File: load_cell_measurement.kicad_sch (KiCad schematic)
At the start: 15 parts, among them IC1 MCP3561R-E_ST, J8 Conn_01x04_Pin

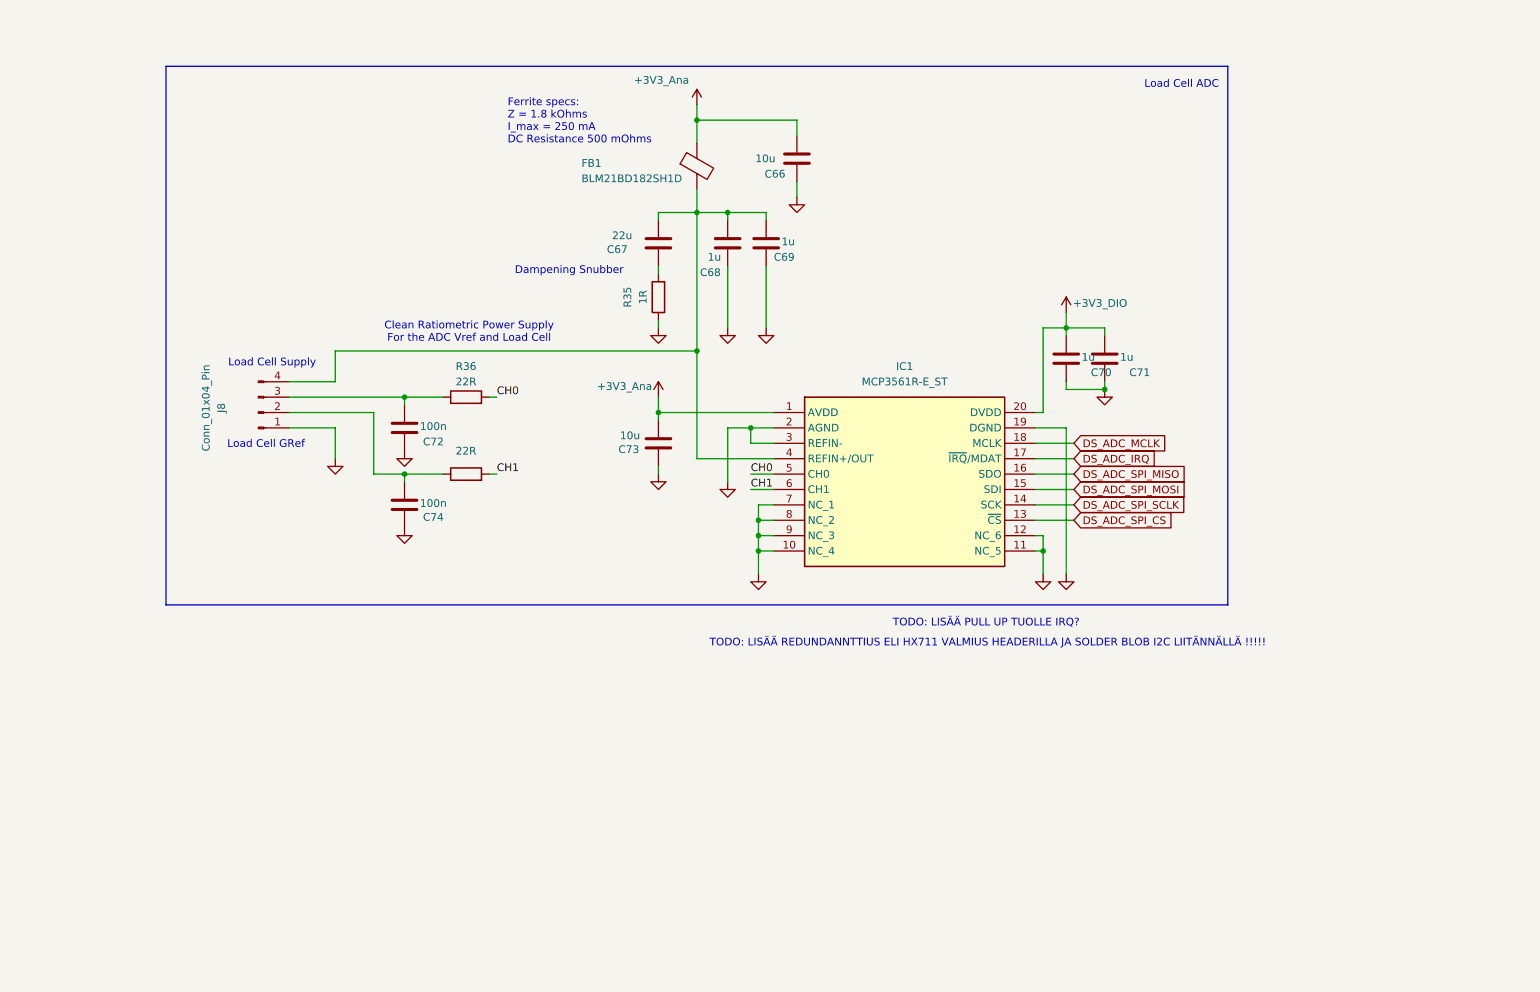
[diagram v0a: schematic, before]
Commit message: Switched isolating opamp. Switched Isolating DCDC converter. Minor layout improvements. Added load cell ADC.
[KiCad Version: 10.0.4]
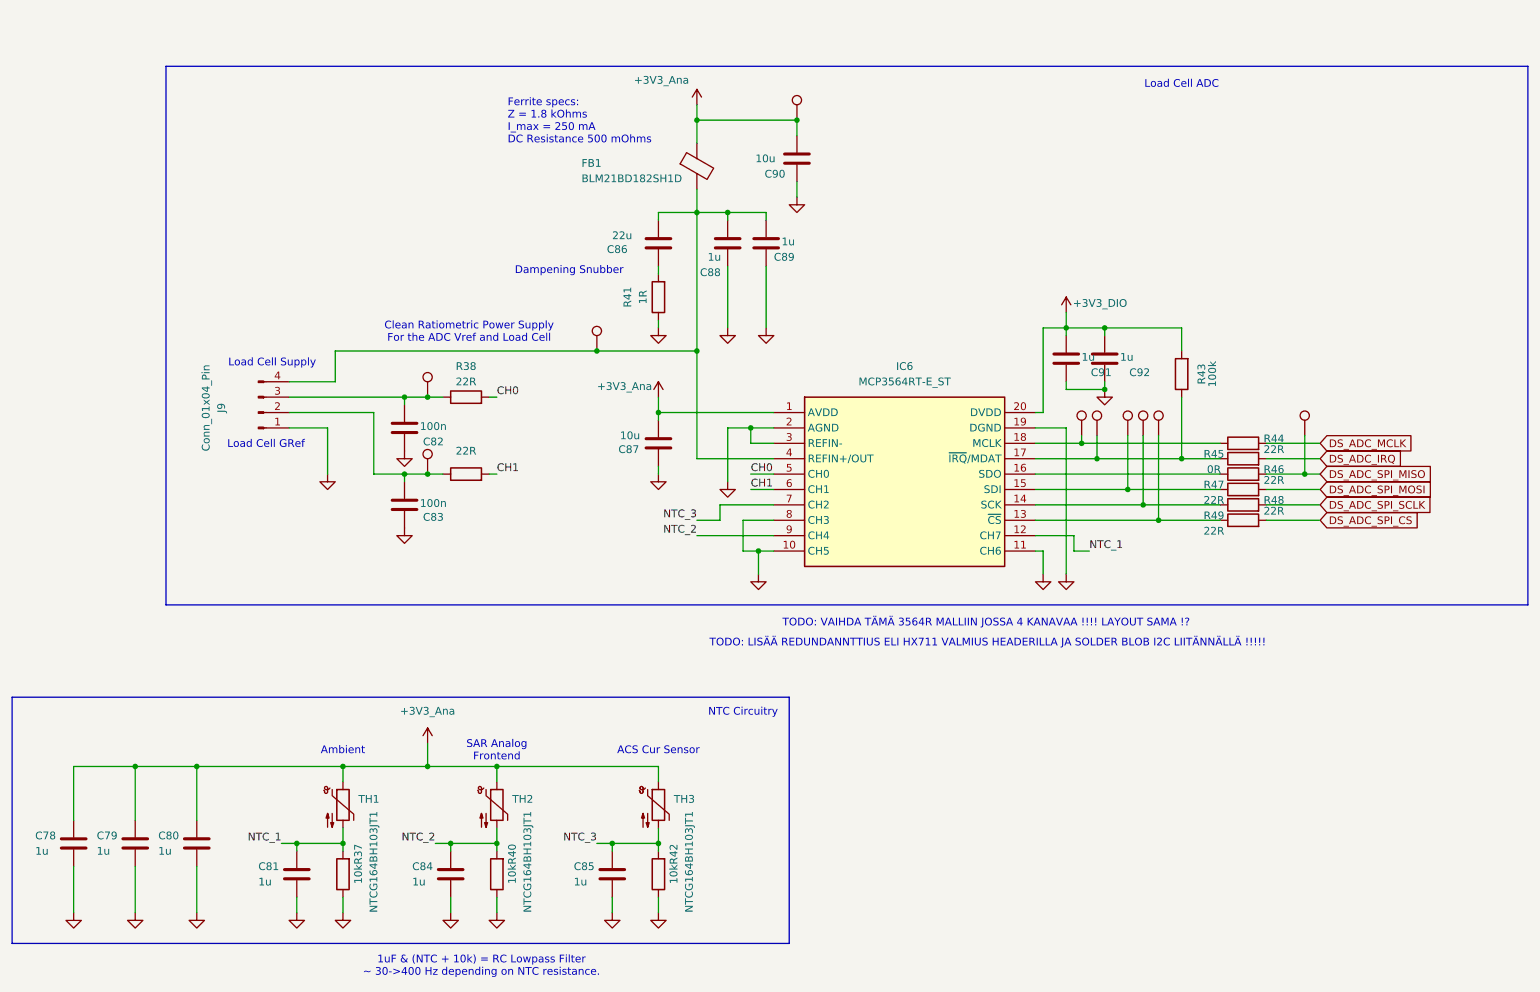
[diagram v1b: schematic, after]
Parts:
- removed IC1: MCP3561R-E_ST, SamacSys_Parts:SOP65P640X120-20N, symbol SamacSys_Parts:MCP3561R-E_ST
- added C78, C79, C80, C81, C84, C85: 1u, Capacitor_SMD:C_0603_1608Metric_Pad1.08x0.95mm_HandSolder, symbol Device:C
- added I1, I10, I2, I3, I4, I5, I6, I7, I8, I9: TestPoint, TestPoint:TestPoint_Pad_D1.0mm, symbol Connector:TestPoint
- added IC6: MCP3564RT-E_ST, SOP65P640X120-20N, symbol SamacSys_Parts:MCP3564RT-E_ST
- added R37, R40, R42: 10k, Resistor_SMD:R_0603_1608Metric_Pad0.98x0.95mm_HandSolder, symbol Device:R
- added R43: 100k, Resistor_SMD:R_0603_1608Metric_Pad0.98x0.95mm_HandSolder, symbol Device:R
- added R44, R46, R47, R48, R49: 22R, Resistor_SMD:R_0603_1608Metric_Pad0.98x0.95mm_HandSolder, symbol Device:R
- added R45: 0R, Resistor_SMD:R_0603_1608Metric_Pad0.98x0.95mm_HandSolder, symbol Device:R
- added TH1, TH2, TH3: NTCG164BH103JT1, Resistor_SMD:R_0603_1608Metric_Pad0.98x0.95mm_HandSolder, symbol Device:Thermistor_NTC
- renumbered C72 to C82, C74 to C83, C67 to C86, C73 to C87, C68 to C88, C69 to C89, C66 to C90, C70 to C91, C71 to C92, J8 to J9, R36 to R38, R37 to R39, R35 to R41
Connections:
- net +3V3_Ana: now also C78.1, C79.1, C80.1, I4.1, IC6.1 (AVDD), TH1.1, TH2.1, TH3.1
- net +3V3_DIO: now also IC6.20 (DVDD), R43.2
- net CH0: now also IC6.5 (CH0)
- net CH1: now also IC6.6 (CH1)
- net DS_ADC_IRQ: now also R45.2
- net DS_ADC_MCLK: now also R44.2
- net DS_ADC_SPI_CS: now also R49.2
- net DS_ADC_SPI_MISO: now also I10.1, R46.2
- net DS_ADC_SPI_MOSI: now also R47.2
- net DS_ADC_SPI_SCLK: now also R48.2
- net GND: now also C78.2, C79.2, C80.2, C81.2, C84.2, C85.2, IC6.10 (CH5), IC6.11 (CH6), IC6.19 (DGND), IC6.2 (AGND), IC6.3 (REFIN-), IC6.8 (CH3), R37.1, R40.1, R42.1
- net at C86.2, C88.2, C89.2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: now also I3.1, IC6.4 (REFIN+/OUT)
- net at C83.2, J9.2 (Pin_2), R39.1: now also I2.1
- net at C82.2, J9.3 (Pin_3), R38.1: now also I1.1
- new net: I6.1, IC6.17 (~{IRQ}/MDAT), R43.1, R45.1
- new net: I8.1, IC6.14 (SCK), R48.1
- new net: I7.1, IC6.15 (SDI), R47.1
- new net: I5.1, IC6.18 (MCLK), R44.1
- new net: I9.1, IC6.13 (~{CS}), R49.1
- new net: IC6.16 (SDO), R46.1
- new net NTC_1: C81.1, IC6.12 (CH7), R37.2, TH1.2
- new net NTC_2: C84.1, IC6.9 (CH4), R40.2, TH2.2
- new net NTC_3: C85.1, IC6.7 (CH2), R42.2, TH3.2
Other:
- note added: "1uF & (NTC + 10k) = RC Lowpass Filter ~ 30->400 Hz depending on NTC resistance."
- note added: "ACS Cur Sensor"
- note added: "Ambient"
- note added: "NTC Circuitry"
- note added: "SAR Analog Frontend"
- note added: "TODO: VAIHDA TÄMÄ 3564R MALLIIN JOSSA 4 KANAVAA !!!! LAYOUT SAMA !?"
- note removed: "TODO: LISÄÄ PULL UP TUOLLE IRQ?"

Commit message: Implemented proper sallen key filter. Add 4V2 LDO Back.
[KiCad Version: 10.0.4]
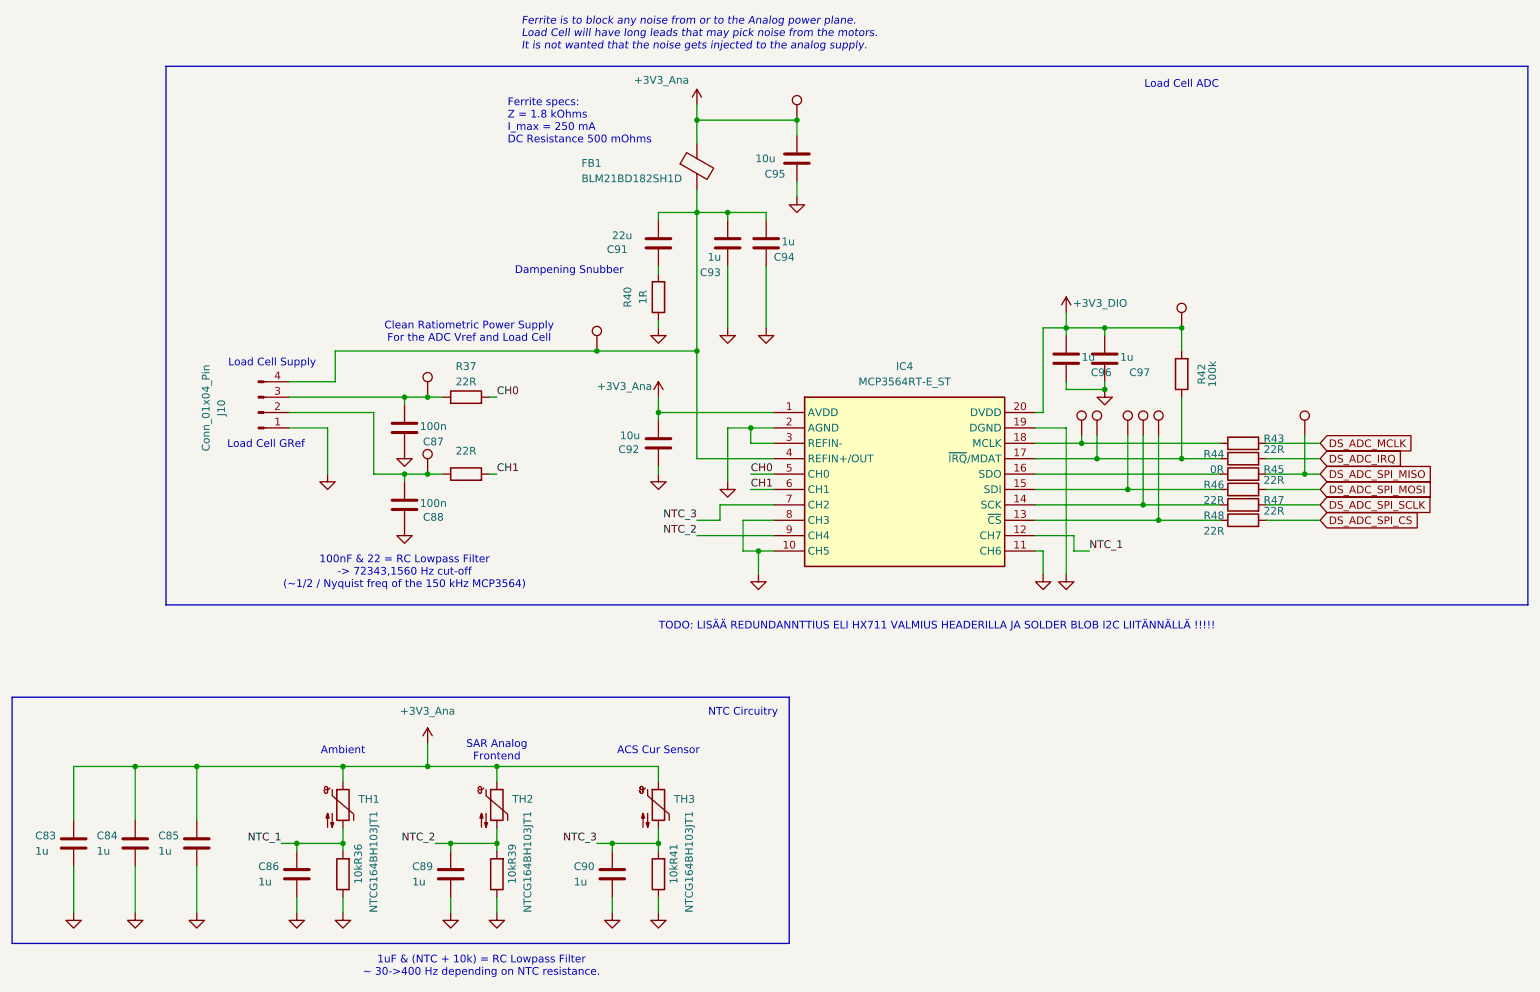
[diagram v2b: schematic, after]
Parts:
- added I?: TestPoint, TestPoint:TestPoint_Pad_D1.0mm, symbol Connector:TestPoint
- renumbered C78 to C83, C79 to C84, C80 to C85, C81 to C86, C82 to C87, C83 to C88, C84 to C89, C85 to C90, C86 to C91, C87 to C92, C88 to C93, C89 to C94, C90 to C95, C91 to C96, C92 to C97, IC6 to IC4, J9 to J10, R37 to R36, R38 to R37, R39 to R38, R40 to R39, R41 to R40, R42 to R41, R43 to R42, R44 to R43, R45 to R44, R46 to R45, R47 to R46, R48 to R47, R49 to R48
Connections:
- net +3V3_DIO: now also I?.1
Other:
- note added: "100nF & 22 = RC Lowpass Filter -> 72343,1560 Hz cut-off (~1/2 / Nyquist freq of the 150 kHz MCP3564)"
- note added: "Ferrite is to block any noise from or to the Analog power plane. Load Cell will have long leads that may pick noise from the motors. It is not wanted that the noise gets injected to the analog supply."
- note removed: "TODO: VAIHDA TÄMÄ 3564R MALLIIN JOSSA 4 KANAVAA !!!! LAYOUT SAMA !?"

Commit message: add buttons. Minor tweaks.
[KiCad Version: 10.0.4]
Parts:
- removed I?: TestPoint, TestPoint:TestPoint_Pad_D1.0mm, symbol Connector:TestPoint
- added I11: TestPoint, TestPoint:TestPoint_Pad_D1.0mm, symbol Connector:TestPoint
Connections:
- net +3V3_DIO: now also I11.1
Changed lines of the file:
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@@
 	)
 	(junction
+		(at 224.79 81.28)
+		(diameter 0)
+		(color 0 0 0 0)
+	)
+	(junction
 		(at 111.76 153.67)
 		(diameter 0)
@@
 		(color 0 0 0 0)
 	)
-	(junction
-		(at 224.79 81.28)
-		(diameter 0)
-		(color 0 0 0 0)
-	)
 	(wire
 		(pts
@@
 	)
 	(symbol
+		(lib_id "Connector:TestPoint")
+		(at 224.79 81.28 0)
+		(mirror y)
+		(unit 1)
+		(body_style 1)
+		(exclude_from_sim no)
+		(in_bom yes)
+		(on_board yes)
+		(in_pos_files yes)
+		(dnp no)
+		(property "Reference" "I11"
+			(at 222.25 78.74 0)
+			(hide yes)
+			(show_name no)
+			(do_not_autoplace no)
+			(effects
+				(font
+					(size 1.27 1.27)
+				)
+				(justify left)
+			)
+		)
+		(property "Value" "TestPoint"
+			(at 222.25 81.28 0)
+			(hide yes)
+			(show_name no)
+			(do_not_autoplace no)
+			(effects
+				(font
+					(size 1.27 1.27)
+				)
+				(justify left)
+			)
+		)
+		(property "Footprint" "TestPoint:TestPoint_Pad_D1.0mm"
+			(at 219.71 81.28 0)
+			(hide yes)
+			(show_name no)
+			(do_not_autoplace no)
+			(effects
+				(font
+					(size 1.27 1.27)
+				)
+			)
+		)
+		(property "Datasheet" ""
+			(at 219.71 81.28 0)
+			(hide yes)
+			(show_name no)
+			(do_not_autoplace no)
+			(effects
+				(font
+					(size 1.27 1.27)
+				)
+			)
+		)
+		(property "Description" "test point"
+			(at 224.79 81.28 0)
+			(hide yes)
+			(show_name no)
+			(do_not_autoplace no)
+			(effects
+				(font
+					(size 1.27 1.27)
+				)
+			)
+		)
+		(property "Manufacturing_Number" ""
+			(at 224.79 81.28 0)
+			(hide yes)
+			(show_name no)
+			(do_not_autoplace no)
+			(effects
+				(font
+					(size 1.27 1.27)
+				)
+			)
+		)
+		(pin "1"
+		)
+		(instances
+			(project "motor_testbench_v1_0"
+				(path "/da638649-102c-44f9-b928-e91cd399cc2f/bd55160d-8c4c-42fa-b0ab-c795a19ea32a"
+					(reference "I11")
+					(unit 1)
+				)
+			)
+		)
+	)
+	(symbol
 		(lib_id "Device:C")
 		(at 130.81 171.45 0)
@@
 					(unit 1)
 				)
-			)
-		)
-	)
-	(symbol
-		(lib_id "Connector:TestPoint")
-		(at 224.79 81.28 0)
-		(mirror y)
-		(unit 1)
-		(body_style 1)
-		(exclude_from_sim no)
-		(in_bom yes)
-		(on_board yes)
-		(in_pos_files yes)
-		(dnp no)
-		(property "Reference" "I?"
-			(at 222.25 78.74 0)
-			(hide yes)
-			(show_name no)
-			(do_not_autoplace no)
-			(effects
-				(font
-					(size 1.27 1.27)
-				)
-				(justify left)
-			)
-		)
-		(property "Value" "TestPoint"
-			(at 222.25 81.28 0)
-			(hide yes)
-			(show_name no)
-			(do_not_autoplace no)
-			(effects
-				(font
-					(size 1.27 1.27)
-				)
-				(justify left)
-			)
-		)
-		(property "Footprint" "TestPoint:TestPoint_Pad_D1.0mm"
-			(at 219.71 81.28 0)
-			(hide yes)
-			(show_name no)
-			(do_not_autoplace no)
-			(effects
-				(font
-					(size 1.27 1.27)
-				)
-			)
-		)
-		(property "Datasheet" ""
-			(at 219.71 81.28 0)
-			(hide yes)
-			(show_name no)
-			(do_not_autoplace no)
-			(effects
-				(font
-					(size 1.27 1.27)
-				)
-			)
-		)
-		(property "Description" "test point"
-			(at 224.79 81.28 0)
-			(hide yes)
-			(show_name no)
-			(do_not_autoplace no)
-			(effects
-				(font
-					(size 1.27 1.27)
-				)
-			)
-		)
-		(property "Manufacturing_Number" ""
-			(at 224.79 81.28 0)
-			(hide yes)
-			(show_name no)
-			(do_not_autoplace no)
-			(effects
-				(font
-					(size 1.27 1.27)
-				)
-			)
-		)
-		(pin "1"
-		)
-		(instances
-			(project "motor_testbench_v1_0"
-				(path "/da638649-102c-44f9-b928-e91cd399cc2f/bd55160d-8c4c-42fa-b0ab-c795a19ea32a"
-					(reference "I?")
-					(unit 1)
-				)
